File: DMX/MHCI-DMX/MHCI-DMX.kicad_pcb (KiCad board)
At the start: 2 copper layers, 79 x 90 mm, 91 parts, among them J1 XLR_Male, J10 Conn_01x02, J11 Conn_01x02, J12 Conn_01x02, J13 Conn_01x02, J14 Conn_01x02, J15 Conn_01x02, J16 Conn_01x04, J17 Conn_01x08, J18 Conn_01x04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

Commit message: Adding 680R bias resistor network
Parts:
- added R6: 680R, Resistor_SMD:R_0402_1005Metric, F.Cu at (97.2, 131.2)
- added R7: 680R, Resistor_SMD:R_0402_1005Metric, F.Cu at (97.2, 128.9)
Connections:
- net /DMX_PASSTHROUGH renamed Net-(D1-A)
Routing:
- net +5V_ISO: track 18.1 -> 35.8 mm, vias 0 -> 1
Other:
- board text added: "DMX Bias"

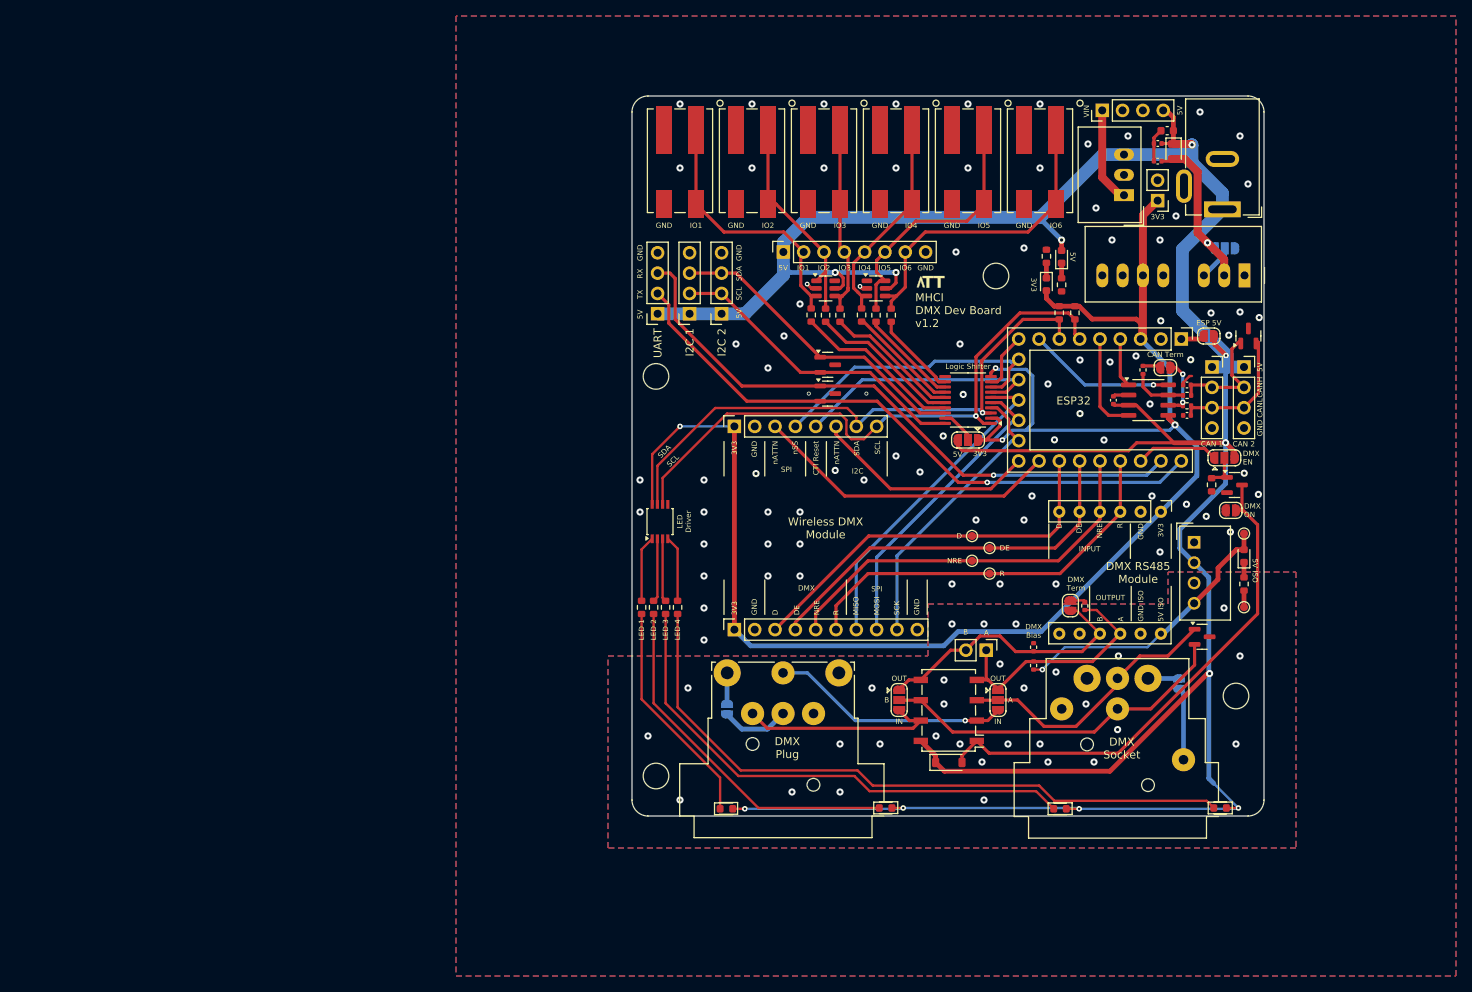
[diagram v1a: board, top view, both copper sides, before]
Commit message: New screen
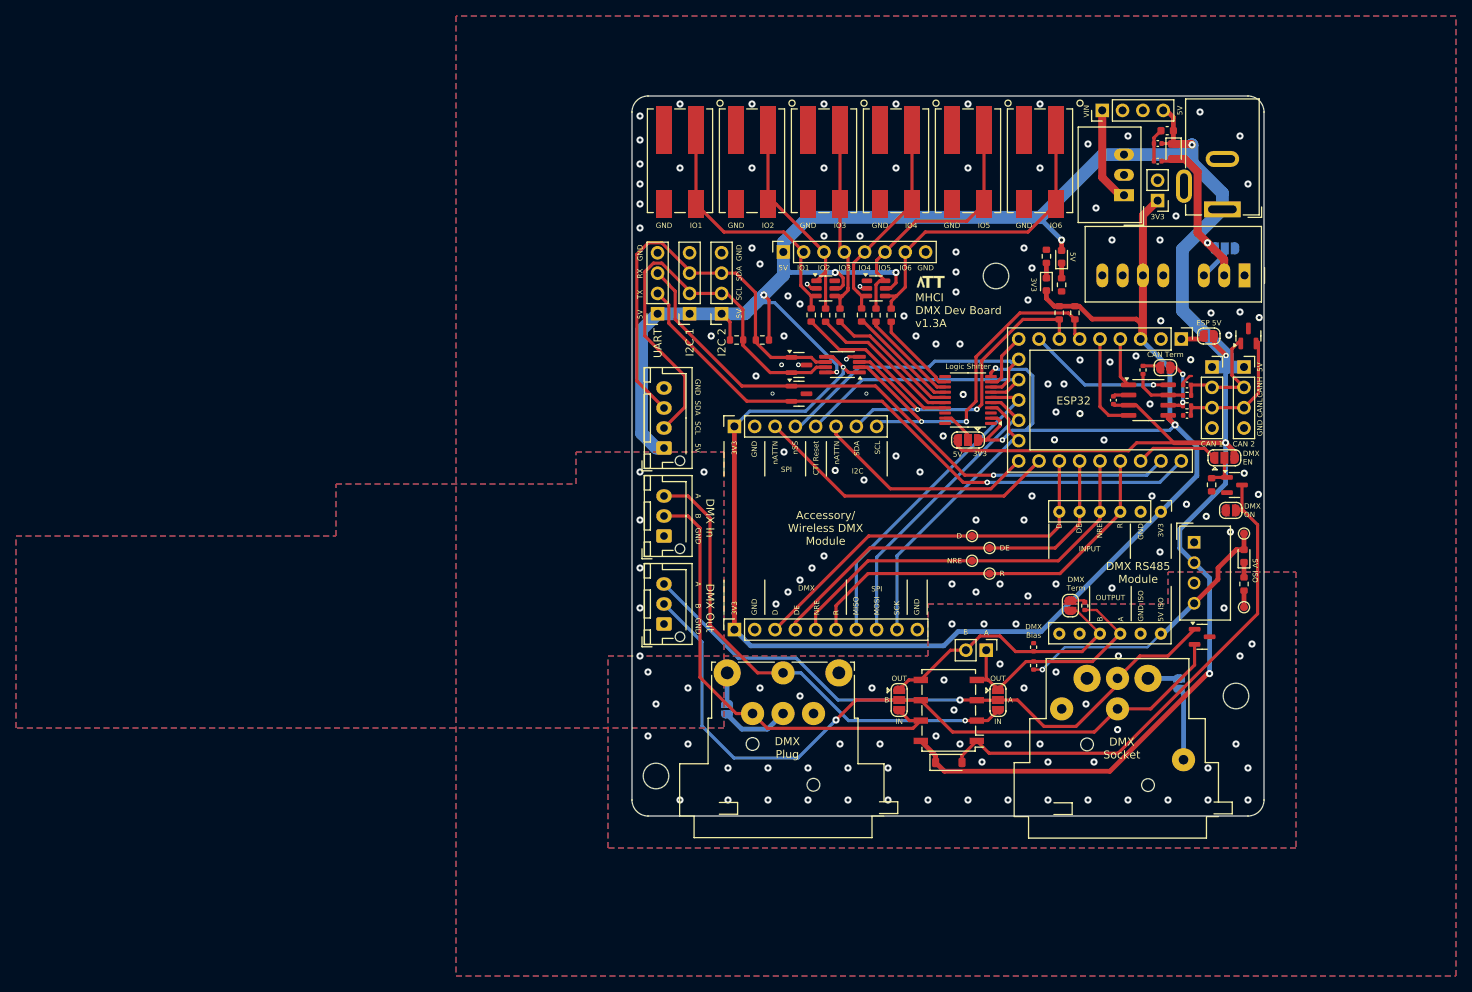
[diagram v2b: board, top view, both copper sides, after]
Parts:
- removed D10, D8: GREEN, LED_SMD:LED_0603_1608Metric
- removed D7, D9: RED, LED_SMD:LED_0603_1608Metric
- removed H3: MountingHole, MountingHole:MountingHole_3.2mm_M3
- removed R12, R13: 300R, Resistor_SMD:R_0603_1608Metric
- removed U8: TXB0108PW, Package_SO:TSSOP-20_4.4x6.5mm_P0.65mm
- added J20: Conn_01x03, Connector_JST:JST_XH_B3B-XH-AM_1x03_P2.50mm_Vertical, F.Cu at (51.0, 126.0)
- added J21: Conn_01x04, Connector_JST:JST_XH_B4B-XH-AM_1x04_P2.50mm_Vertical, F.Cu at (51.0, 104.0)
- added J9: Conn_01x03, Connector_JST:JST_XH_B3B-XH-AM_1x03_P2.50mm_Vertical, F.Cu at (51.0, 115.0)
- added U12: TCA9517ADGK, Package_SO:VSSOP-8_3x3mm_P0.65mm, F.Cu at (73.3, 93.6)
- R10, R11: value 300R -> 4K7
- U2: value ~ -> TXS0108EPW; footprint Package_SO:TSSOP-8_3x3mm_P0.65mm -> Package_SO:TSSOP-20_4.4x6.5mm_P0.65mm
- moved U2 41.4 mm to (89.0, 98.0), turned to 180 degrees
- moved R10 36.7 mm to (63.3, 90.5), turned to 180 degrees
- moved R11 35.0 mm to (60.1, 90.5), turned to 0 degrees
- moved D3 3.59 mm to (67.9, 93.6)
- moved D6 3.59 mm to (67.9, 97.2)
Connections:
- R10 pad 1: Net-(D7-K) -> +5V
- R10 pad 2: Net-(U2-LED0) -> SDA_5
- R11 pad 1: Net-(D8-K) -> +5V
- R11 pad 2: Net-(U2-LED1) -> SCL_5
- R17 pad 1: Net-(U8-B3) -> Net-(U2-B3)
- R18 pad 1: Net-(U8-B4) -> Net-(U2-B4)
- R19 pad 1: Net-(U8-B5) -> Net-(U2-B5)
- R20 pad 1: Net-(U8-B6) -> Net-(U2-B6)
- R21 pad 1: Net-(U8-B7) -> Net-(U2-B7)
- R22 pad 1: Net-(U8-B8) -> Net-(U2-B8)
- U2 pad 1: Net-(U2-LED0) -> unconnected-(U2-A1-Pad1)
- U2 pad 2: Net-(U2-LED1) -> +3V3
- U2 pad 3: Net-(U2-LED2) -> unconnected-(U2-A2-Pad3)
- U2 pad 4: Net-(U2-LED3) -> GPIO_X1
- U2 pad 5: GND -> GPIO_X2
- U2 pad 6: SCL -> GPIO_X3
- U2 pad 7: SDA -> CTI_RESET
- U2 pad 8: +3V3 -> GPIO_X5
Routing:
- net Net-(D10-K): track 83.9 -> 0.00 mm
- net Net-(D9-K): track 65.1 -> 0.00 mm
- net /B_OUT: track 44.6 -> 91.2 mm, vias 0 -> 1
- net /A_OUT: track 34.1 -> 79.2 mm, vias 0 -> 1
- net Net-(D8-K): track 44.8 -> 0.00 mm
- net +5V: track 374.1 -> 332.6 mm, vias 11 -> 9
- net /B_IN: track 25.4 -> 57.7 mm
- net /A_IN: track 29.9 -> 61.8 mm
- net Net-(D7-K): track 28.4 -> 0.00 mm
- net SCL: track 76.7 -> 48.3 mm, vias 1 -> 2
- net SDA: track 72.9 -> 46.3 mm, vias 1 -> 2
- net Net-(U8-B3): track 21.2 -> 0.00 mm
- net Net-(U2-B3): track 0.00 -> 21.2 mm
- net Net-(U8-B4): track 19.3 -> 0.00 mm
- net Net-(U2-B4): track 0.00 -> 19.3 mm
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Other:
- board text added: "Accessory/ Wireless DMX Module"
- board text added: "DMX In"
- board text added: "DMX Out"
- board text added: "MHCI DMX Dev Board v1.3A"
- board text removed: "LED 1"
- board text removed: "LED 2"
- board text removed: "LED 3"
- board text removed: "LED 4"
- board text removed: "LED Driver"
- board text removed: "MHCI DMX Dev Board v1.2"
- board text removed: "Wireless DMX Module"
